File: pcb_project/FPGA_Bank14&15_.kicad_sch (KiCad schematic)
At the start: 39 parts, among them IC3 IS61WV204816BLL-10TLI, IC4 IS61WV204816BLL-10TLI, U1 XC7A100T-FTG256, U9 MT25QL128ABA1ESE-0SIT

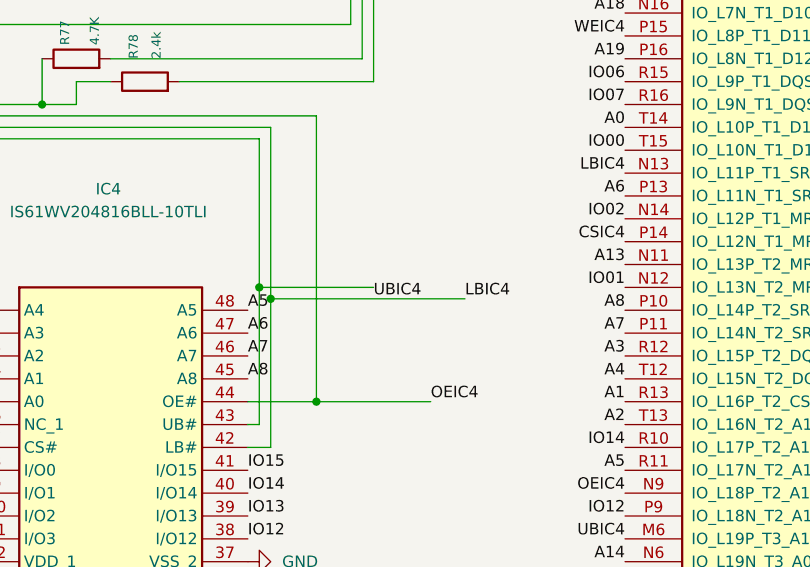
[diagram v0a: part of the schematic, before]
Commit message: Clean up FPGA pins, and other small improvements
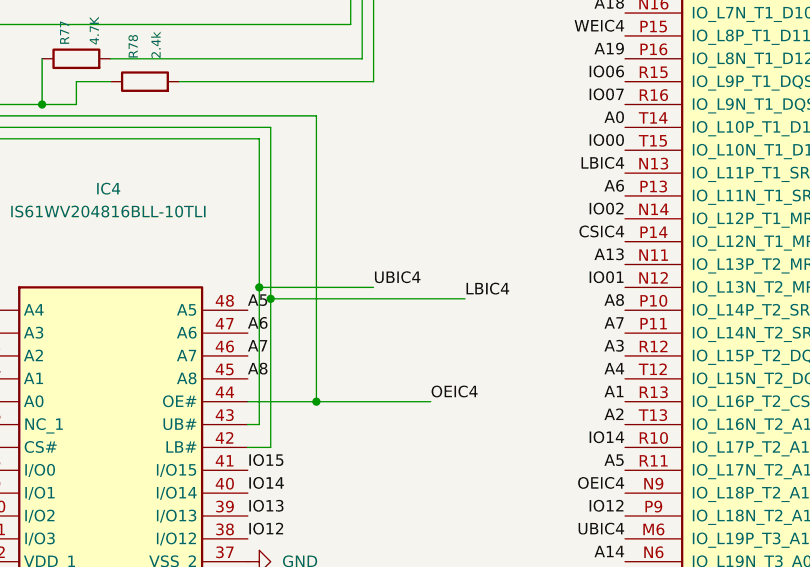
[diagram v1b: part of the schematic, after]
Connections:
- net LBIC4: no longer U1.M6 (IO_L19P_T3_A10_D26_14)
- net UBIC4: now reaches IC4.43 (UB#), R69.2
- net UBIC4: now also U1.M6 (IO_L19P_T3_A10_D26_14)
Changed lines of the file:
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@@
 	)
 	(label "UBIC4"
-		(at 158.75 148.59 0)
+		(at 158.75 147.32 0)
 		(effects
 			(font

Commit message: FLASH Pcb layout
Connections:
- net J13: now reaches R76.1, U9.7 (DQ3/HOLD#)
- net J13: now also U1.J13 (IO_L1P_T0_D00_MOSI_14); no longer U1.K16 (IO_L2N_T0_D03_14)
- net K15: now reaches R78.2, U9.1 (S#)
- net K15: now also U1.K15 (IO_L2P_T0_D02_14); no longer U1.L12 (IO_L6P_T0_FCS_B_14)
- net L12: now reaches U9.5 (DQ0)
- net L12: now also U1.L12 (IO_L6P_T0_FCS_B_14); no longer U1.J13 (IO_L1P_T0_D00_MOSI_14)
- net J14: now reaches U1.J14 (IO_L1N_T0_D01_DIN_14)
- net J14: now also R77.2, U9.3 (W#/DQ2); no longer U9.2 (DQ1)
- new net K16: U1.K16 (IO_L2N_T0_D03_14), U9.2 (DQ1)
- no-connect marks 14 -> 15
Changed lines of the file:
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@@
 	)
 	(junction
+		(at 158.75 109.22)
+		(diameter 0)
+		(color 0 0 0 0)
+	)
+	(junction
 		(at 129.54 69.85)
 		(diameter 0)
@@
 	)
 	(junction
-		(at 158.75 109.22)
-		(diameter 0)
-		(color 0 0 0 0)
-	)
-	(junction
 		(at 320.04 60.96)
 		(diameter 0)
@@
 	)
 	(no_connect
+		(at 186.69 81.28)
+	)
+	(no_connect
 		(at 306.07 118.11)
 	)
@@
 	(wire
 		(pts
-			(xy 97.79 91.44) (xy 186.69 91.44)
-		)
-		(stroke
-			(width 0)
-			(type default)
-		)
-	)
-	(wire
-		(pts
 			(xy 320.04 71.12) (xy 320.04 74.93)
 		)
@@
 	(wire
 		(pts
-			(xy 158.75 109.22) (xy 186.69 109.22)
-		)
-		(stroke
-			(width 0)
-			(type default)
-		)
-	)
-	(wire
-		(pts
 			(xy 314.96 71.12) (xy 314.96 76.2)
 		)
@@
 	(wire
 		(pts
-			(xy 158.75 88.9) (xy 186.69 88.9)
+			(xy 114.3 118.11) (xy 156.21 118.11)
 		)
 		(stroke
@@
 	(wire
 		(pts
-			(xy 114.3 118.11) (xy 156.21 118.11)
+			(xy 158.75 109.22) (xy 163.83 109.22)
 		)
 		(stroke
@@
 	(wire
 		(pts
-			(xy 160.02 106.68) (xy 160.02 86.36)
-		)
-		(stroke
-			(width 0)
-			(type default)
-		)
-	)
-	(wire
-		(pts
 			(xy 125.73 127) (xy 121.92 127)
 		)
@@
 	(wire
 		(pts
+			(xy 158.75 93.98) (xy 163.83 93.98)
+		)
+		(stroke
+			(width 0)
+			(type default)
+		)
+	)
+	(wire
+		(pts
 			(xy 158.75 124.46) (xy 137.16 124.46)
 		)
@@
 	(wire
 		(pts
-			(xy 95.25 83.82) (xy 186.69 83.82)
-		)
-		(stroke
-			(width 0)
-			(type default)
-		)
-	)
-	(wire
-		(pts
 			(xy 91.44 66.04) (xy 91.44 69.85)
 		)
@@
 	(wire
 		(pts
-			(xy 160.02 86.36) (xy 186.69 86.36)
-		)
-		(stroke
-			(width 0)
-			(type default)
-		)
-	)
-	(wire
-		(pts
-			(xy 158.75 104.14) (xy 158.75 88.9)
+			(xy 158.75 93.98) (xy 158.75 104.14)
 		)
 		(stroke
@@
 		)
 	)
+	(label "K16"
+		(at 186.69 91.44 180)
+		(effects
+			(font
+				(size 1.27 1.27)
+			)
+			(justify right bottom)
+		)
+	)
 	(label "A0"
 		(at 260.35 116.84 0)
@@
 		)
 	)
+	(label "K16"
+		(at 160.02 106.68 0)
+		(effects
+			(font
+				(size 1.27 1.27)
+			)
+			(justify left bottom)
+		)
+	)
 	(label "OE"
 		(at 300.99 189.23 0)
@@
 		)
 	)
+	(label "K15"
+		(at 186.69 88.9 180)
+		(effects
+			(font
+				(size 1.27 1.27)
+			)
+			(justify right bottom)
+		)
+	)
 	(label "A2"
 		(at 260.35 127 0)
@@
 		)
 	)
+	(label "K15"
+		(at 163.83 109.22 0)
+		(effects
+			(font
+				(size 1.27 1.27)
+			)
+			(justify left bottom)
+		)
+	)
+	(label "J14"
+		(at 186.69 86.36 180)
+		(effects
+			(font
+				(size 1.27 1.27)
+			)
+			(justify right bottom)
+		)
+	)
 	(label "A14"
 		(at 260.35 195.58 0)
@@
 		)
 	)
+	(label "L12"
+		(at 95.25 83.82 0)
+		(effects
+			(font
+				(size 1.27 1.27)
+			)
+			(justify left bottom)
+		)
+	)
 	(label "A10"
 		(at 186.69 205.74 180)
@@
 		)
 	)
+	(label "J13"
+		(at 97.79 91.44 0)
+		(effects
+			(font
+				(size 1.27 1.27)
+			)
+			(justify left bottom)
+		)
+	)
 	(label "A6"
 		(at 144.78 152.4 0)
@@
 		)
 	)
+	(label "J14"
+		(at 163.83 93.98 0)
+		(effects
+			(font
+				(size 1.27 1.27)
+			)
+			(justify left bottom)
+		)
+	)
 	(label "WEIC4"
 		(at 105.41 189.23 180)
@@
 		)
 	)
+	(label "L12"
+		(at 186.69 109.22 180)
+		(effects
+			(font
+				(size 1.27 1.27)
+			)
+			(justify right bottom)
+		)
+	)
 	(label "IO12"
 		(at 144.78 175.26 0)
@@
 		)
 	)
+	(label "J13"
+		(at 186.69 83.82 180)
+		(effects
+			(font
+				(size 1.27 1.27)
+			)
+			(justify right bottom)
+		)
+	)

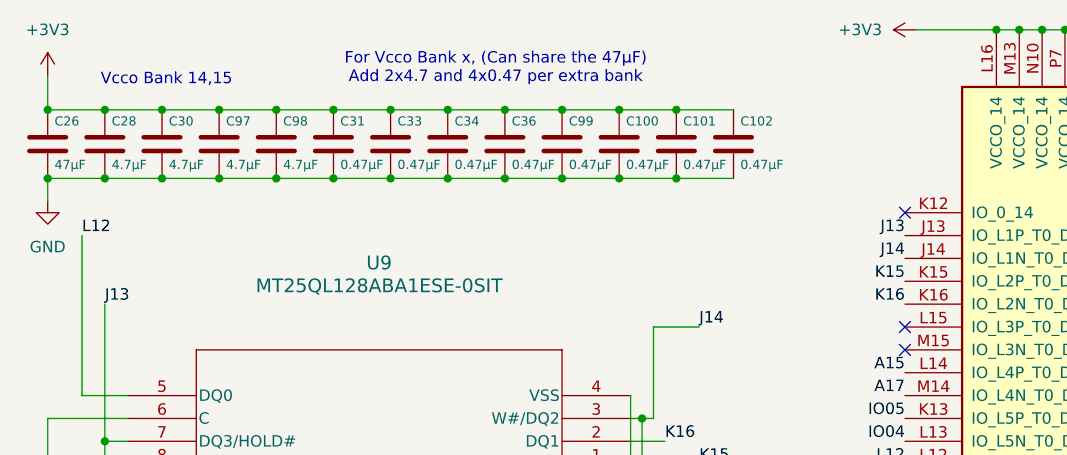
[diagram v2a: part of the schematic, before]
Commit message: FPGA power and grround own vias
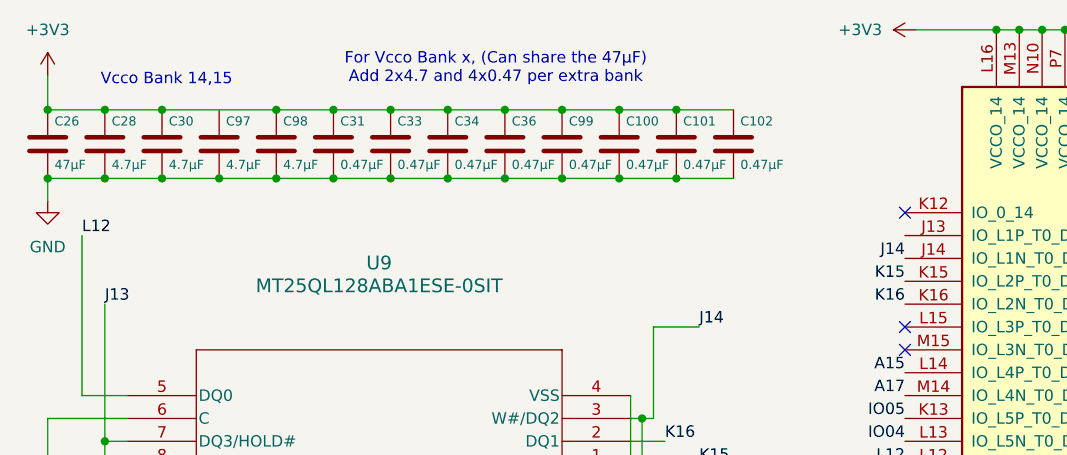
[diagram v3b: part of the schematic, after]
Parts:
- C100, C101, C102, C31, C33, C34, C36, C99: footprint Capacitor_SMD:C_0603_1608Metric_Pad1.08x0.95mm_HandSolder -> Capacitor_SMD:C_01005_0402Metric_Pad0.57x0.30mm_HandSolder
- C28, C30, C97, C98: footprint Capacitor_SMD:C_0805_2012Metric_Pad1.18x1.45mm_HandSolder -> Capacitor_SMD:C_0402_1005Metric_Pad0.74x0.62mm_HandSolder
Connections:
- net +3V3: no longer C97.1
- net J13: no longer U1.J13 (IO_L1P_T0_D00_MOSI_14)
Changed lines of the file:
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@@
 	)
 	(junction
-		(at 110.49 69.85)
-		(diameter 0)
-		(color 0 0 0 0)
-	)
-	(junction
 		(at 161.29 69.85)
 		(diameter 0)
@@
 	(wire
 		(pts
-			(xy 110.49 69.85) (xy 116.84 69.85)
-		)
-		(stroke
-			(width 0)
-			(type default)
-		)
-	)
-	(wire
-		(pts
 			(xy 204.47 60.96) (xy 207.01 60.96)
 		)
@@
 	(wire
 		(pts
-			(xy 104.14 69.85) (xy 110.49 69.85)
+			(xy 104.14 69.85) (xy 116.84 69.85)
 		)
 		(stroke
@@
 		)
 	)
-	(label "J13"
-		(at 186.69 83.82 180)
-		(effects
-			(font
-				(size 1.27 1.27)
-			)
-			(justify right bottom)
-		)
-	)
 	(label "LB"
 		(at 356.87 120.65 0)
@@
 			)
 		)
-		(property "Footprint" "Capacitor_SMD:C_0805_2012Metric_Pad1.18x1.45mm_HandSolder"
+		(property "Footprint" "Capacitor_SMD:C_0402_1005Metric_Pad0.74x0.62mm_HandSolder"
 			(at 117.8052 77.47 0)
 			(effects
@@
 			)
 		)
-		(property "Footprint" "Capacitor_SMD:C_0603_1608Metric_Pad1.08x0.95mm_HandSolder"
+		(property "Footprint" "Capacitor_SMD:C_01005_0402Metric_Pad0.57x0.30mm_HandSolder"
 			(at 143.2052 77.47 0)
 			(effects
@@
 			)
 		)
-		(property "Footprint" "Capacitor_SMD:C_0805_2012Metric_Pad1.18x1.45mm_HandSolder"
+		(property "Footprint" "Capacitor_SMD:C_0402_1005Metric_Pad0.74x0.62mm_HandSolder"
 			(at 111.4552 77.47 0)
 			(effects
@@
 			)
 		)
-		(property "Footprint" "Capacitor_SMD:C_0805_2012Metric_Pad1.18x1.45mm_HandSolder"
+		(property "Footprint" "Capacitor_SMD:C_0402_1005Metric_Pad0.74x0.62mm_HandSolder"
 			(at 105.1052 77.47 0)
 			(effects
@@
 			)
 		)
-		(property "Footprint" "Capacitor_SMD:C_0603_1608Metric_Pad1.08x0.95mm_HandSolder"
+		(property "Footprint" "Capacitor_SMD:C_01005_0402Metric_Pad0.57x0.30mm_HandSolder"
 			(at 124.1552 77.47 0)
 			(effects
@@
 			)
 		)
-		(property "Footprint" "Capacitor_SMD:C_0805_2012Metric_Pad1.18x1.45mm_HandSolder"
+		(property "Footprint" "Capacitor_SMD:C_0402_1005Metric_Pad0.74x0.62mm_HandSolder"
 			(at 98.7552 77.47 0)
 			(effects
@@
 			)
 		)
-		(property "Footprint" "Capacitor_SMD:C_0603_1608Metric_Pad1.08x0.95mm_HandSolder"
+		(property "Footprint" "Capacitor_SMD:C_01005_0402Metric_Pad0.57x0.30mm_HandSolder"
 			(at 130.5052 77.47 0)
 			(effects
@@
 			)
 		)
-		(property "Footprint" "Capacitor_SMD:C_0603_1608Metric_Pad1.08x0.95mm_HandSolder"
+		(property "Footprint" "Capacitor_SMD:C_01005_0402Metric_Pad0.57x0.30mm_HandSolder"
 			(at 149.5552 77.47 0)
 			(effects
@@
 			)
 		)
-		(property "Footprint" "Capacitor_SMD:C_0603_1608Metric_Pad1.08x0.95mm_HandSolder"
+		(property "Footprint" "Capacitor_SMD:C_01005_0402Metric_Pad0.57x0.30mm_HandSolder"
 			(at 162.2552 77.47 0)
 			(effects
@@
 			)
 		)
-		(property "Footprint" "Capacitor_SMD:C_0603_1608Metric_Pad1.08x0.95mm_HandSolder"
+		(property "Footprint" "Capacitor_SMD:C_01005_0402Metric_Pad0.57x0.30mm_HandSolder"
 			(at 155.9052 77.47 0)
 			(effects
@@
 			)
 		)
-		(property "Footprint" "Capacitor_SMD:C_0603_1608Metric_Pad1.08x0.95mm_HandSolder"
+		(property "Footprint" "Capacitor_SMD:C_01005_0402Metric_Pad0.57x0.30mm_HandSolder"
 			(at 136.8552 77.47 0)
 			(effects
@@
 			)
 		)
-		(property "Footprint" "Capacitor_SMD:C_0603_1608Metric_Pad1.08x0.95mm_HandSolder"
+		(property "Footprint" "Capacitor_SMD:C_01005_0402Metric_Pad0.57x0.30mm_HandSolder"
 			(at 168.6052 77.47 0)
 			(effects

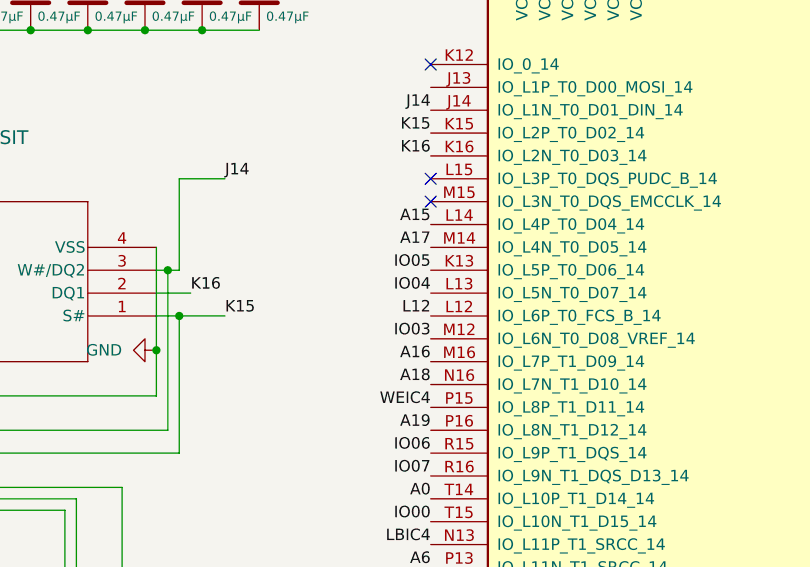
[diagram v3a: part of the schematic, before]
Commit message: Set net class that allows for 2x wires between FPGA balls
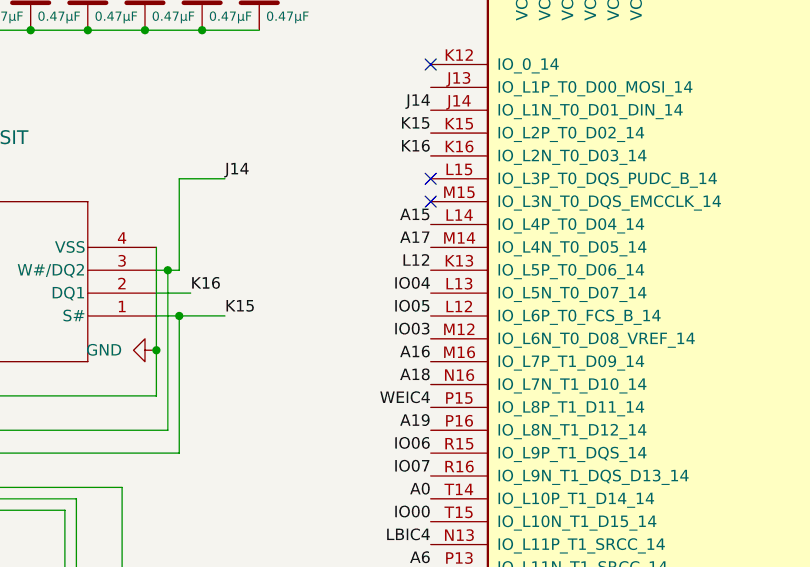
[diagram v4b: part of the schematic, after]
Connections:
- net IO05: now also U1.L12 (IO_L6P_T0_FCS_B_14); no longer U1.K13 (IO_L5P_T0_D06_14)
- net L12: now also U1.K13 (IO_L5P_T0_D06_14); no longer U1.L12 (IO_L6P_T0_FCS_B_14)
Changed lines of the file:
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@@
 		)
 	)
-	(label "IO05"
+	(label "L12"
 		(at 186.69 104.14 180)
 		(effects
@@
 		)
 	)
-	(label "L12"
+	(label "IO05"
 		(at 186.69 109.22 180)
 		(effects

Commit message: Working out from the center of FPGA. Hopes and dreams gambit accepted
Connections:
- no-connect marks 15 -> 16
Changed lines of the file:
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@@
+	)
+	(no_connect
+		(at 186.69 83.82)
 	)
 	(no_connect

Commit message: Changed capacitor sizes. Now it's even more difficult
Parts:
- C100, C101, C102, C31, C33, C34, C36, C99: footprint Capacitor_SMD:C_01005_0402Metric_Pad0.57x0.30mm_HandSolder -> Capacitor_SMD:C_0603_1608Metric_Pad1.08x0.95mm_HandSolder
- C28, C30, C97, C98: footprint Capacitor_SMD:C_0402_1005Metric_Pad0.74x0.62mm_HandSolder -> Capacitor_SMD:C_0603_1608Metric_Pad1.08x0.95mm_HandSolder
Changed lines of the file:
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@@
 			)
 		)
-		(property "Footprint" "Capacitor_SMD:C_0402_1005Metric_Pad0.74x0.62mm_HandSolder"
+		(property "Footprint" "Capacitor_SMD:C_0603_1608Metric_Pad1.08x0.95mm_HandSolder"
 			(at 117.8052 77.47 0)
 			(effects
@@
 			)
 		)
-		(property "Footprint" "Capacitor_SMD:C_01005_0402Metric_Pad0.57x0.30mm_HandSolder"
+		(property "Footprint" "Capacitor_SMD:C_0603_1608Metric_Pad1.08x0.95mm_HandSolder"
 			(at 143.2052 77.47 0)
 			(effects
@@
 			)
 		)
-		(property "Footprint" "Capacitor_SMD:C_0402_1005Metric_Pad0.74x0.62mm_HandSolder"
+		(property "Footprint" "Capacitor_SMD:C_0603_1608Metric_Pad1.08x0.95mm_HandSolder"
 			(at 111.4552 77.47 0)
 			(effects
@@
 			)
 		)
-		(property "Footprint" "Capacitor_SMD:C_0402_1005Metric_Pad0.74x0.62mm_HandSolder"
+		(property "Footprint" "Capacitor_SMD:C_0603_1608Metric_Pad1.08x0.95mm_HandSolder"
 			(at 105.1052 77.47 0)
 			(effects
@@
 			)
 		)
-		(property "Footprint" "Capacitor_SMD:C_01005_0402Metric_Pad0.57x0.30mm_HandSolder"
+		(property "Footprint" "Capacitor_SMD:C_0603_1608Metric_Pad1.08x0.95mm_HandSolder"
 			(at 124.1552 77.47 0)
 			(effects
@@
 			)
 		)
-		(property "Footprint" "Capacitor_SMD:C_0402_1005Metric_Pad0.74x0.62mm_HandSolder"
+		(property "Footprint" "Capacitor_SMD:C_0603_1608Metric_Pad1.08x0.95mm_HandSolder"
 			(at 98.7552 77.47 0)
 			(effects
@@
 			)
 		)
-		(property "Footprint" "Capacitor_SMD:C_01005_0402Metric_Pad0.57x0.30mm_HandSolder"
+		(property "Footprint" "Capacitor_SMD:C_0603_1608Metric_Pad1.08x0.95mm_HandSolder"
 			(at 130.5052 77.47 0)
 			(effects
@@
 			)
 		)
-		(property "Footprint" "Capacitor_SMD:C_01005_0402Metric_Pad0.57x0.30mm_HandSolder"
+		(property "Footprint" "Capacitor_SMD:C_0603_1608Metric_Pad1.08x0.95mm_HandSolder"
 			(at 149.5552 77.47 0)
 			(effects
@@
 			)
 		)
-		(property "Footprint" "Capacitor_SMD:C_01005_0402Metric_Pad0.57x0.30mm_HandSolder"
+		(property "Footprint" "Capacitor_SMD:C_0603_1608Metric_Pad1.08x0.95mm_HandSolder"
 			(at 162.2552 77.47 0)
 			(effects
@@
 			)
 		)
-		(property "Footprint" "Capacitor_SMD:C_01005_0402Metric_Pad0.57x0.30mm_HandSolder"
+		(property "Footprint" "Capacitor_SMD:C_0603_1608Metric_Pad1.08x0.95mm_HandSolder"
 			(at 155.9052 77.47 0)
 			(effects
@@
 			)
 		)
-		(property "Footprint" "Capacitor_SMD:C_01005_0402Metric_Pad0.57x0.30mm_HandSolder"
+		(property "Footprint" "Capacitor_SMD:C_0603_1608Metric_Pad1.08x0.95mm_HandSolder"
 			(at 136.8552 77.47 0)
 			(effects
@@
 			)
 		)
-		(property "Footprint" "Capacitor_SMD:C_01005_0402Metric_Pad0.57x0.30mm_HandSolder"
+		(property "Footprint" "Capacitor_SMD:C_0603_1608Metric_Pad1.08x0.95mm_HandSolder"
 			(at 168.6052 77.47 0)
 			(effects

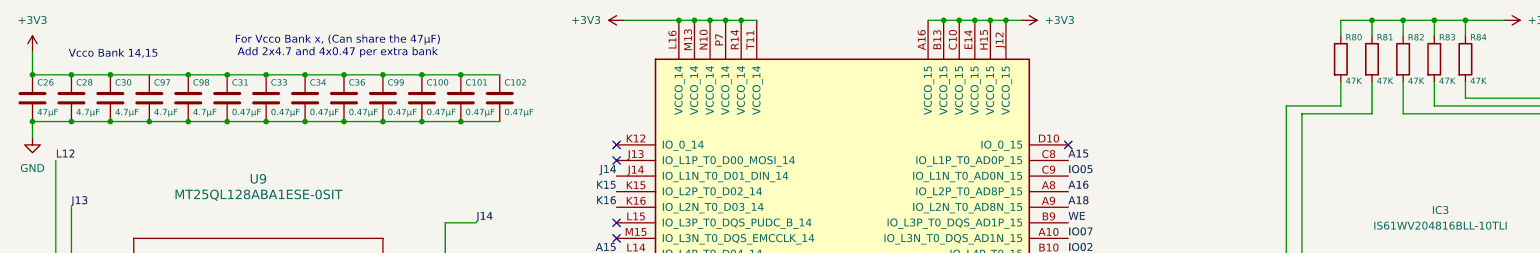
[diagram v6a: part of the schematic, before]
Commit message: Fix remaining FPGA capasitors
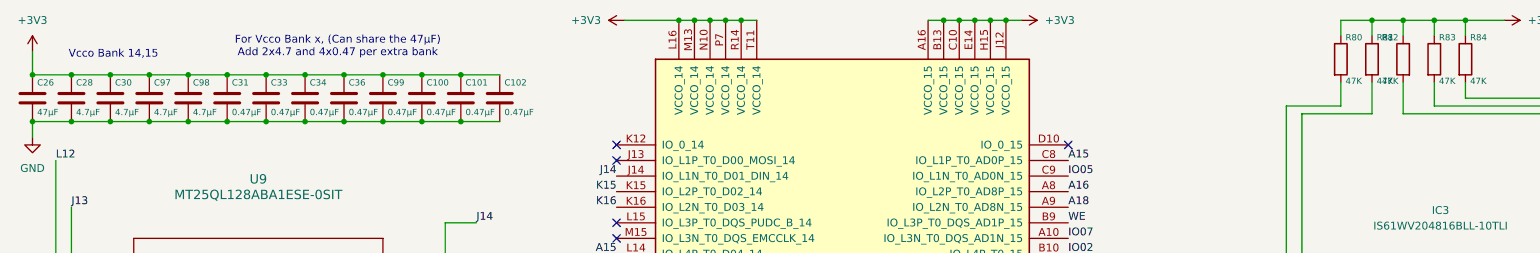
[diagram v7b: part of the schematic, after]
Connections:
- net +3V3: now also C97.1
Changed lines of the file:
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@@
 	)
 	(junction
+		(at 110.49 69.85)
+		(diameter 0)
+		(color 0 0 0 0)
+	)
+	(junction
 		(at 104.14 69.85)
 		(diameter 0)
@@
 	(wire
 		(pts
+			(xy 110.49 69.85) (xy 116.84 69.85)
+		)
+		(stroke
+			(width 0)
+			(type default)
+		)
+	)
+	(wire
+		(pts
 			(xy 80.01 130.81) (xy 146.05 130.81)
 		)
@@
 	(wire
 		(pts
-			(xy 104.14 69.85) (xy 116.84 69.85)
+			(xy 104.14 69.85) (xy 110.49 69.85)
 		)
 		(stroke
@@
 		(lib_id "Device:R")
 		(at 314.96 67.31 0)
+		(mirror y)
 		(unit 1)
 		(exclude_from_sim no)
@@
 		(dnp no)
 		(property "Reference" "R82"
-			(at 315.722 63.754 0)
+			(at 314.198 63.754 0)
 			(effects
 				(font
@@
 		)
 		(property "Value" "47K"
-			(at 315.722 70.866 0)
+			(at 314.198 70.866 0)
 			(effects
 				(font
@@
 		)
 		(property "Footprint" "Resistor_SMD:R_0805_2012Metric_Pad1.20x1.40mm_HandSolder"
-			(at 313.182 67.31 90)
+			(at 316.738 67.31 90)
 			(effects
 				(font
